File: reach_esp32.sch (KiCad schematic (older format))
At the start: 45 parts

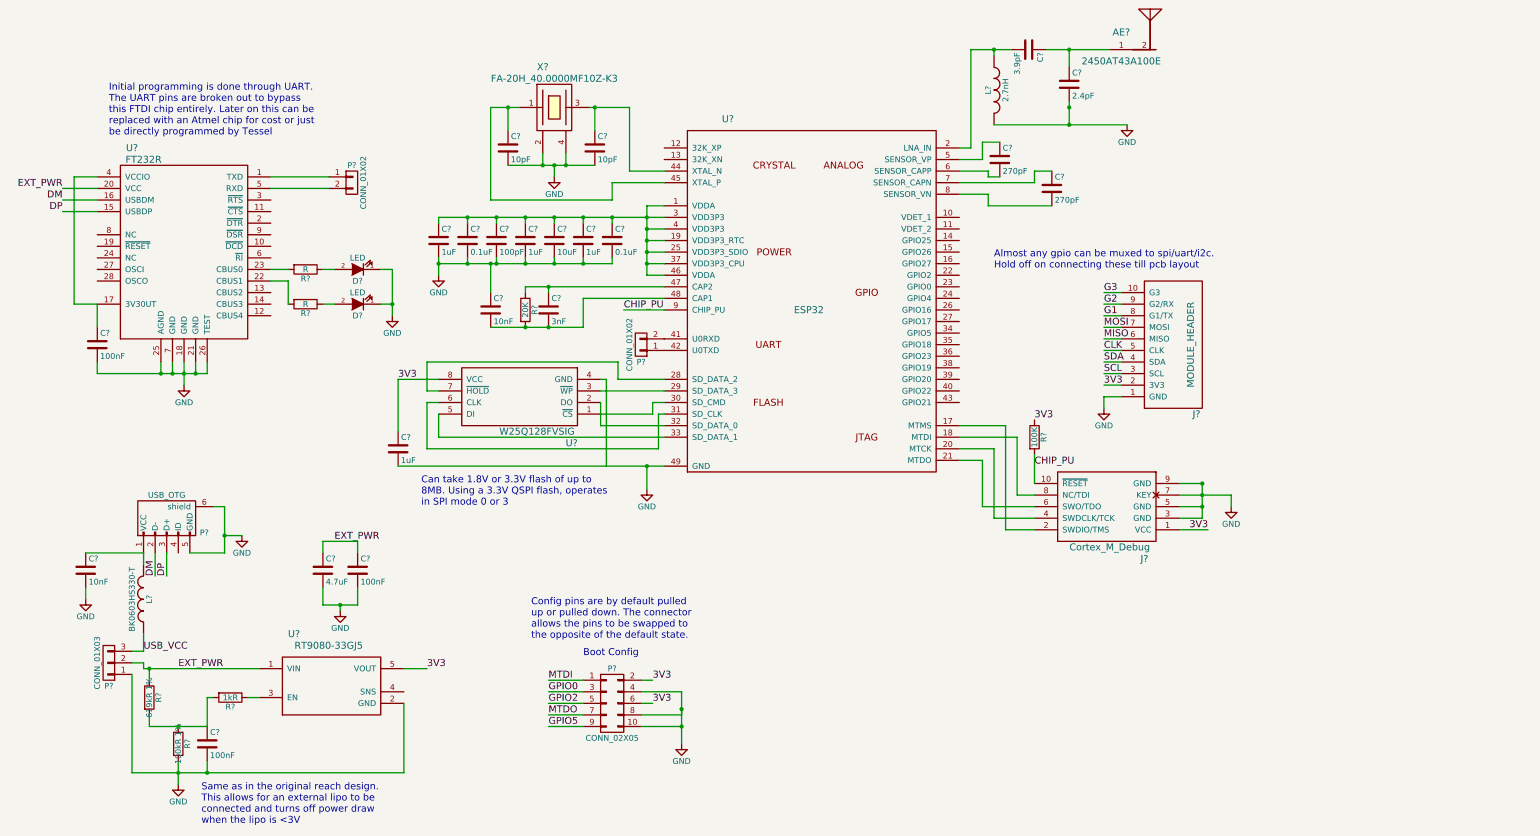
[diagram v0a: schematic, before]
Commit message: adding caps
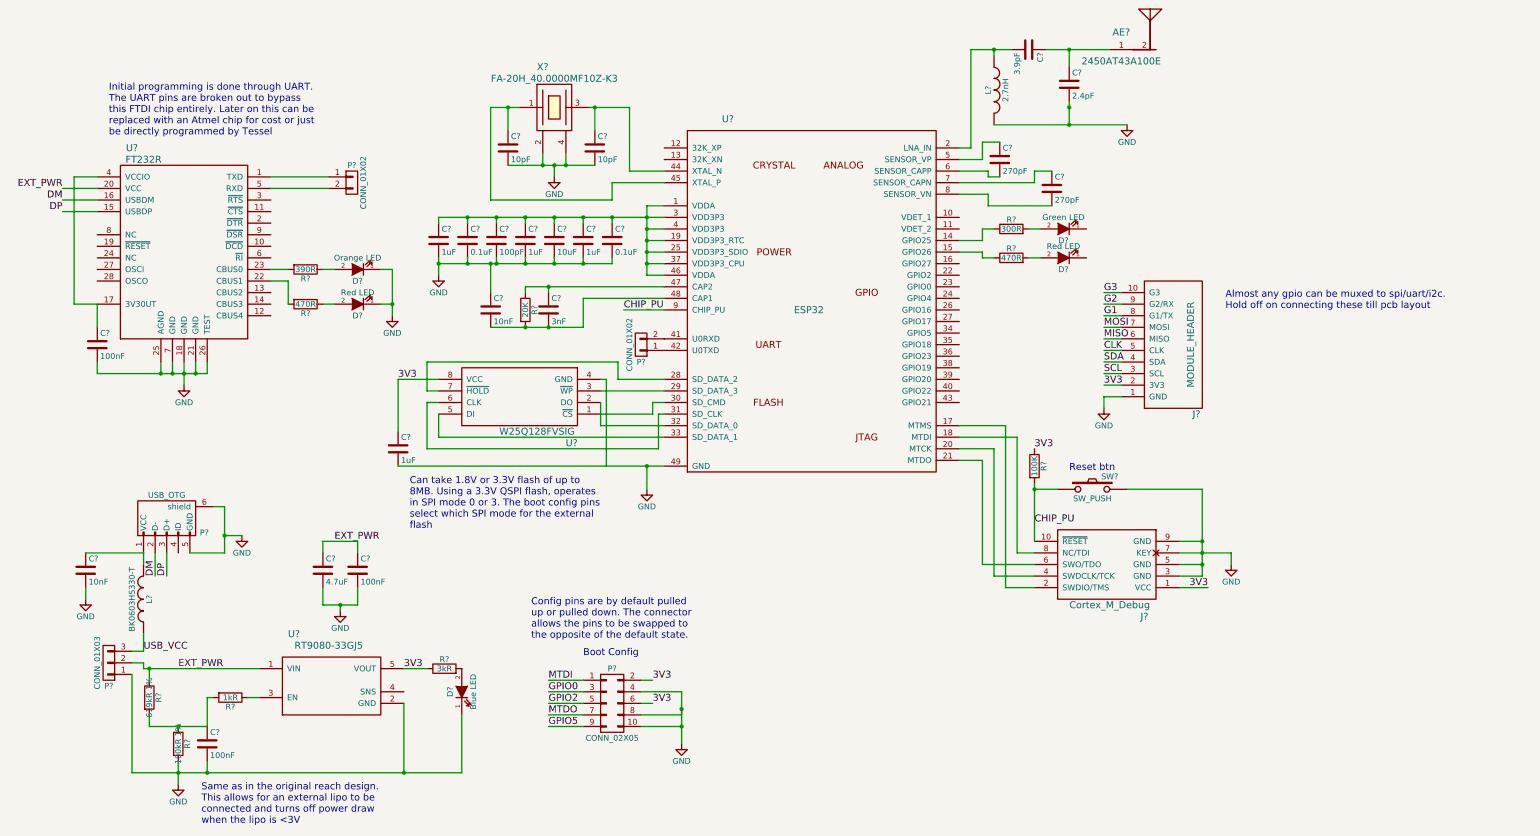
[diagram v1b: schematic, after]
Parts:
- added D?: Blue LED, symbol LED
- added D?: Green LED, symbol LED
- added D?: Red LED, symbol LED
- added R?: 3kR, symbol R
- added R?: 300R, symbol R
- added R?: 470R, symbol R
- added SW?: SW_PUSH, symbol SW_PUSH
- C?: footprint (none) -> Capacitors_SMD:C_0402
- D?: value LED -> Orange LED
- D?: value LED -> Red LED
- R?: value R -> 390R
- R?: value R -> 470R
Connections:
- net 3V3: now also R?.1
- net CHIP_PU: now also SW?.1
- net GND: now also D?.1 (K), SW?.2
- net at U?.14 (GPIO25): now also R?.1
- net at U?.15 (GPIO26): now also R?.1
- new net: D?.2 (A), R?.2 (x3)
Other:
- note added: "Can take 1.8V or 3.3V flash of up to\n8MB. Using a 3.3V QSPI flash, operates\nin SPI mode 0 or 3. The boot config pins\nselect which SPI mode for the external \nflash"
- note added: "Reset btn"
- note removed: "Can take 1.8V or 3.3V flash of up to\n8MB. Using a 3.3V QSPI flash, operates\nin SPI mode 0 or 3"
- moved on the sheet: J?, R?
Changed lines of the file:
@@
 P 3450 2850
 F 0 "D?" H 3450 2950 50  0000 C CNN
-F 1 "LED" H 3450 2750 50  0000 C CNN
+F 1 "Orange LED" H 3450 2750 50  0000 C CNN
 F 2 "" H 3450 2850 50  0000 C CNN
 F 3 "" H 3450 2850 50  0000 C CNN
@@
 P 3450 3150
 F 0 "D?" H 3450 3250 50  0000 C CNN
-F 1 "LED" H 3450 3050 50  0000 C CNN
+F 1 "Red LED" H 3450 3050 50  0000 C CNN
 F 2 "" H 3450 3150 50  0000 C CNN
 F 3 "" H 3450 3150 50  0000 C CNN
@@
 P 3000 2850
 F 0 "R?" V 3080 2850 50  0000 C CNN
-F 1 "R" V 3000 2850 50  0000 C CNN
+F 1 "390R" V 3000 2850 50  0000 C CNN
 F 2 "" V 2930 2850 50  0000 C CNN
 F 3 "" H 3000 2850 50  0000 C CNN
@@
 P 3000 3150
 F 0 "R?" V 3080 3150 50  0000 C CNN
-F 1 "R" V 3000 3150 50  0000 C CNN
+F 1 "470R" V 3000 3150 50  0000 C CNN
 F 2 "" V 2930 3150 50  0000 C CNN
 F 3 "" H 3000 3150 50  0000 C CNN
@@
 F 0 "C?" H 1225 3600 50  0000 L CNN
 F 1 "100nF" H 1225 3400 50  0000 L CNN
-F 2 "" H 1238 3350 50  0000 C CNN
-F 3 "" H 1200 3500 50  0000 C CNN
+F 2 "Capacitors_SMD:C_0402" H 1238 3350 50  0001 C CNN
+F 3 "http://www.digikey.com/product-detail/en/LMK105BJ104KV-F/587-1227-1-ND/931004" H 1200 3500 50  0001 C CNN
 	1    1200 3500
 	1    0    0    -1
@@
 Text Label 3250 5200 0    60   ~ 0
 EXT_PWR
-Text Label 4050 6300 0    60   ~ 0
+Text Label 3850 6300 0    60   ~ 0
 3V3
 Text Label 3800 3800 0    60   ~ 0
@@
 L Cortex_M_Debug J?
 U 1 1 57F0685A
-P 9950 4900
-F 0 "J?" H 9650 5350 60  0000 C CNN
-F 1 "Cortex_M_Debug" H 9950 5250 60  0000 C CNN
-F 2 "" H 9750 4900 60  0001 C CNN
-F 3 "" H 9750 4900 60  0001 C CNN
-	1    9950 4900
+P 9950 5400
+F 0 "J?" H 9650 5850 60  0000 C CNN
+F 1 "Cortex_M_Debug" H 9950 5750 60  0000 C CNN
+F 2 "" H 9750 5400 60  0001 C CNN
+F 3 "" H 9750 5400 60  0001 C CNN
+	1    9950 5400
 	-1   0    0    1
 $EndComp
-Text Label 10800 5100 2    60   ~ 0
+Text Label 10800 5600 2    60   ~ 0
 3V3
 $Comp
 L GND #PWR?
 U 1 1 57F07162
-P 11000 4900
-F 0 "#PWR?" H 11000 4650 50  0001 C CNN
-F 1 "GND" H 11000 4750 50  0000 C CNN
-F 2 "" H 11000 4900 50  0000 C CNN
-F 3 "" H 11000 4900 50  0000 C CNN
-	1    11000 4900
+P 11000 5400
+F 0 "#PWR?" H 11000 5150 50  0001 C CNN
+F 1 "GND" H 11000 5250 50  0000 C CNN
+F 2 "" H 11000 5400 50  0000 C CNN
+F 3 "" H 11000 5400 50  0000 C CNN
+	1    11000 5400
 	1    0    0    -1
 $EndComp
@@
 	2600 6550 2500 6550
 Wire Wire Line
-	1500 7200 3850 7200
+	1500 7200 4350 7200
 Wire Wire Line
 	1900 7100 1900 7300
@@
 Connection ~ 6250 6800
 Wire Wire Line
-	10550 5100 10800 5100
-Wire Wire Line
-	10750 5000 10550 5000
-Wire Wire Line
-	10750 4700 10750 5000
-Wire Wire Line
-	10750 4900 10550 4900
-Wire Wire Line
-	10550 4800 11000 4800
-Connection ~ 10750 4900
-Wire Wire Line
-	10750 4700 10550 4700
-Connection ~ 10750 4800
-Connection ~ 10750 4700
-Wire Wire Line
-	11000 4800 11000 4900
+	10550 5600 10800 5600
+Wire Wire Line
+	10750 5500 10550 5500
+Wire Wire Line
+	10750 4750 10750 5500
+Wire Wire Line
+	10750 5400 10550 5400
+Wire Wire Line
+	10550 5300 11000 5300
+Connection ~ 10750 5400
+Wire Wire Line
+	10750 5200 10550 5200
+Connection ~ 10750 5300
+Connection ~ 10750 5200
+Wire Wire Line
+	11000 5300 11000 5400
 Wire Wire Line
 	8650 4200 9050 4200
 Wire Wire Line
-	9050 4200 9050 5100
-Wire Wire Line
-	9050 5100 9300 5100
+	9050 4200 9050 5600
+Wire Wire Line
+	9050 5600 9300 5600
 Wire Wire Line
 	8650 4300 9150 4300
 Wire Wire Line
-	9150 4300 9150 4800
-Wire Wire Line
-	9150 4800 9300 4800
+	9150 4300 9150 5300
+Wire Wire Line
+	9150 5300 9300 5300
 Wire Wire Line
 	8650 4400 8950 4400
 Wire Wire Line
-	8950 4400 8950 5000
-Wire Wire Line
-	8950 5000 9300 5000
-Wire Wire Line
-	9300 4900 8850 4900
-Wire Wire Line
-	8850 4900 8850 4500
+	8950 4400 8950 5500
+Wire Wire Line
+	8950 5500 9300 5500
+Wire Wire Line
+	8850 5400 9300 5400
+Wire Wire Line
+	8850 4500 8850 5400
 Wire Wire Line
 	8850 4500 8650 4500
@@
 	5750 3200 6100 3200
 Wire Wire Line
-	9300 4450 9300 4700
+	9300 4700 9300 5200
 $Comp
 L R R?
 U 1 1 57F089E1
-P 9300 4300
-F 0 "R?" V 9380 4300 50  0000 C CNN
-F 1 "100K" V 9300 4300 50  0000 C CNN
-F 2 "" V 9230 4300 50  0000 C CNN
-F 3 "" H 9300 4300 50  0000 C CNN
-	1    9300 4300
-	1    0    0    -1
-$EndComp
-Text Label 9300 4550 0    60   ~ 0
+P 9300 4550
+F 0 "R?" V 9380 4550 50  0000 C CNN
+F 1 "100K" V 9300 4550 50  0000 C CNN
+F 2 "" V 9230 4550 50  0000 C CNN
+F 3 "" H 9300 4550 50  0000 C CNN
+	1    9300 4550
+	1    0    0    -1
+$EndComp
+Text Label 9300 5050 0    60   ~ 0
 CHIP_PU
-Text Label 9300 4150 0    60   ~ 0
+Text Label 9300 4400 0    60   ~ 0
 3V3
 $Comp
@@
 Text Notes 4950 6050 0    60   ~ 0
 Config pins are by default pulled\nup or pulled down. The connector\nallows the pins to be swapped to\nthe opposite of the default state.
-Text Notes 4000 4900 0    60   ~ 0
-Can take 1.8V or 3.3V flash of up to\n8MB. Using a 3.3V QSPI flash, operates\nin SPI mode 0 or 3
+Text Notes 3900 5100 0    60   ~ 0
+Can take 1.8V or 3.3V flash of up to\n8MB. Using a 3.3V QSPI flash, operates\nin SPI mode 0 or 3. The boot config pins\nselect which SPI mode for the external \nflash
 Text Notes 1300 1700 0    60   ~ 0
 Initial programming is done through UART.\nThe UART pins are broken out to bypass \nthis FTDI chip entirely. Later on this can be\nreplaced with an Atmel chip for cost or just\nbe directly programmed by Tessel
-Text Notes 8950 2850 0    60   ~ 0
+Text Notes 10950 3200 0    60   ~ 0
 Almost any gpio can be muxed to spi/uart/i2c.\nHold off on connecting these till pcb layout
+$Comp
+L LED D?
+U 1 1 57F42F99
+P 4350 6500
+F 0 "D?" H 4350 6600 50  0000 C CNN
+F 1 "Blue LED" H 4350 6400 50  0000 C CNN
+F 2 "" H 4350 6500 50  0000 C CNN
+F 3 "http://www.digikey.com/product-detail/en/LB%20Q39G-L2N2-35-1/475-2816-1-ND/2176355" H 4350 6500 50  0001 C CNN
+	1    4350 6500
+	0    -1   -1   0
+$EndComp
+$Comp
+L R R?
+U 1 1 57F43497
+P 4200 6300
+F 0 "R?" V 4280 6300 50  0000 C CNN
+F 1 "3kR" V 4200 6300 50  0000 C CNN
+F 2 "" V 4130 6300 50  0000 C CNN
+F 3 "" H 4200 6300 50  0000 C CNN
+	1    4200 6300
+	0    -1   -1   0
+$EndComp
+$Comp
+L LED D?
+U 1 1 57F4437D
+P 9550 2500
+F 0 "D?" H 9550 2600 50  0000 C CNN
+F 1 "Green LED" H 9550 2400 50  0000 C CNN
+F 2 "" H 9550 2500 50  0000 C CNN
+F 3 "" H 9550 2500 50  0000 C CNN
+	1    9550 2500
+	-1   0    0    1
+$EndComp
+$Comp
+L R R?
+U 1 1 57F4466B
+P 9100 2500
+F 0 "R?" V 9180 2500 50  0000 C CNN
+F 1 "300R" V 9100 2500 50  0000 C CNN
+F 2 "" V 9030 2500 50  0000 C CNN
+F 3 "" H 9100 2500 50  0000 C CNN
+	1    9100 2500
+	0    -1   -1   0
+$EndComp
+$Comp
+L R R?
+U 1 1 57F44C73
+P 9100 2750
+F 0 "R?" V 9180 2750 50  0000 C CNN
+F 1 "470R" V 9100 2750 50  0000 C CNN
+F 2 "" V 9030 2750 50  0000 C CNN
+F 3 "" H 9100 2750 50  0000 C CNN
+	1    9100 2750
+	0    -1   -1   0
+$EndComp
+$Comp
+L LED D?
+U 1 1 57F44D24
+P 9550 2750
+F 0 "D?" H 9550 2850 50  0000 C CNN
+F 1 "Red LED" H 9550 2650 50  0000 C CNN
+F 2 "" H 9550 2750 50  0000 C CNN
+F 3 "" H 9550 2750 50  0000 C CNN
+	1    9550 2750
+	-1   0    0    1
+$EndComp
+$Comp
+L SW_PUSH SW?
+U 1 1 57F44FD0
+P 9800 4750
+F 0 "SW?" H 9950 4860 50  0000 C CNN
+F 1 "SW_PUSH" H 9800 4670 50  0000 C CNN
+F 2 "" H 9800 4750 50  0000 C CNN
+F 3 "" H 9800 4750 50  0000 C CNN
+	1    9800 4750
+	1    0    0    -1
+$EndComp
+Wire Wire Line
+	4350 7200 4350 6700
+Connection ~ 3850 7200
+Wire Wire Line
+	8650 2600 8850 2600
+Wire Wire Line
+	8850 2600 8850 2500
+Wire Wire Line
+	8850 2500 8950 2500
+Wire Wire Line
+	8650 2700 8850 2700
+Wire Wire Line
+	8850 2700 8850 2750
+Wire Wire Line
+	8850 2750 8950 2750
+Wire Wire Line
+	9250 2500 9350 2500
+Wire Wire Line
+	9250 2750 9350 2750
+Wire Wire Line
+	9500 4750 9300 4750
+Connection ~ 9300 4750
+Wire Wire Line
+	10100 4750 10750 4750
+Text Notes 9600 4600 0    60   ~ 0
+Reset btn
 $EndSCHEMATC
